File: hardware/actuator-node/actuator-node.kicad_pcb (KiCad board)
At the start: 2 copper layers, 70 x 60 mm, 60 parts, among them J1 PHASES, J2 CAN IN, J3 CAN EXT, J4 19V IN, J5 SWD, J6 ENCODER, J7 NTC, J8 SPI, U1 STM32G431CBT6, U2 SN65HVD230, U4 INA240A1D, U5 INA240A1D, U6 AMS1117-3.3, Y1 8 MHz

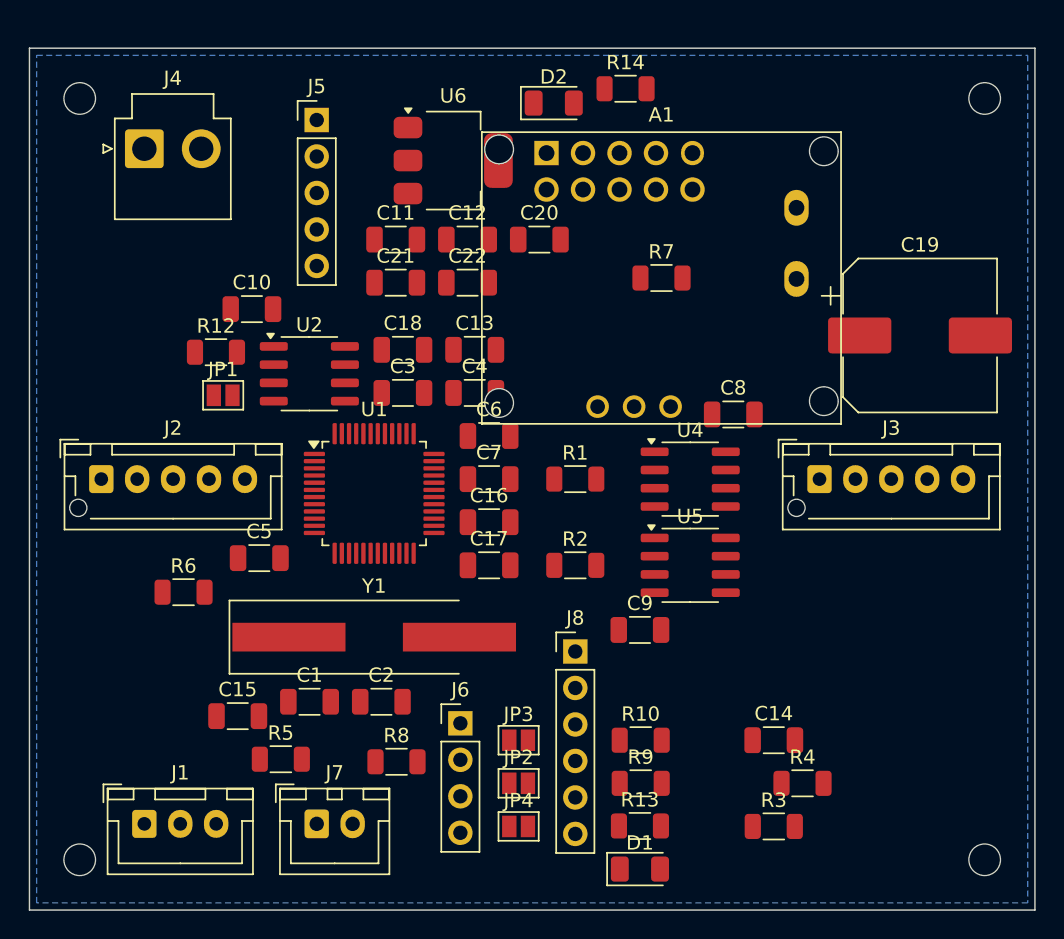
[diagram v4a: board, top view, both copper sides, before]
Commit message: Lay the node out around right-angle connectors, and spec what it can do
The connector order is all right-angle JST: 3-pin XH, 5-pin XH and 2-pin VH,
with no 2-pin XH at all. A right-angle body opens toward +Y at 0 degrees, so
the rotation is what points a cable off the board, and the placer had no
concept of rotation - it put J2 through the crystal and pushed J1 and J7 past
the outline.

kigen.rotate_boxes turns a footprint's courtyard with it; pinned entries now
take an optional third element; check.py rotates the library courtyard before
testing overlap and outline, and verifies the angle as well as the position.

Floorplan, following the three placement rules:
  - CAN on opposite edges, J2 left and J3 right
  - the whole motor loom on the bottom edge: phases, NTC, encoder, SPI
  - power and SWD on the top
All eight ports are on the perimeter, none closer than 1.1 mm to an edge.

Four things the auto-placer got wrong and are now pinned:
  - U6 sat under the driver module, stacking the LDO's heat under the bridge's
  - R7 sat on A1's exact origin; it belongs under the module, but deliberately
    placed clear of every pad rather than by accident
  - both crystal load caps sat at one end of a 20 mm hand-solder footprint,
    leaving one of them 22 mm from its terminal
  - the node-ID pull-ups were stranded 13 mm from their jumpers

Vbus divider R4 4k7 -> 10k. 100 k / 4k7 read 19 V as 0.85 V, a quarter of the
ADC span. 100 k / 10 k reads 1.73 V and clips at 36 V.

Two renderer bugs, both only visible once something was rotated or mirrored:
  - pad angles were being summed with the footprint angle, but KiCad stores a
    pad's angle absolutely
  - the mirror reflected about the origin rather than the view box, and the
    substrate rect took its min in board space instead of screen space, so the
    bottom view sat 13 mm left and grew a slab off the far edge

New docs:
  - docs/capabilities.md - bus range, torque and current resolution, loop
    rates, CAN bandwidth a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
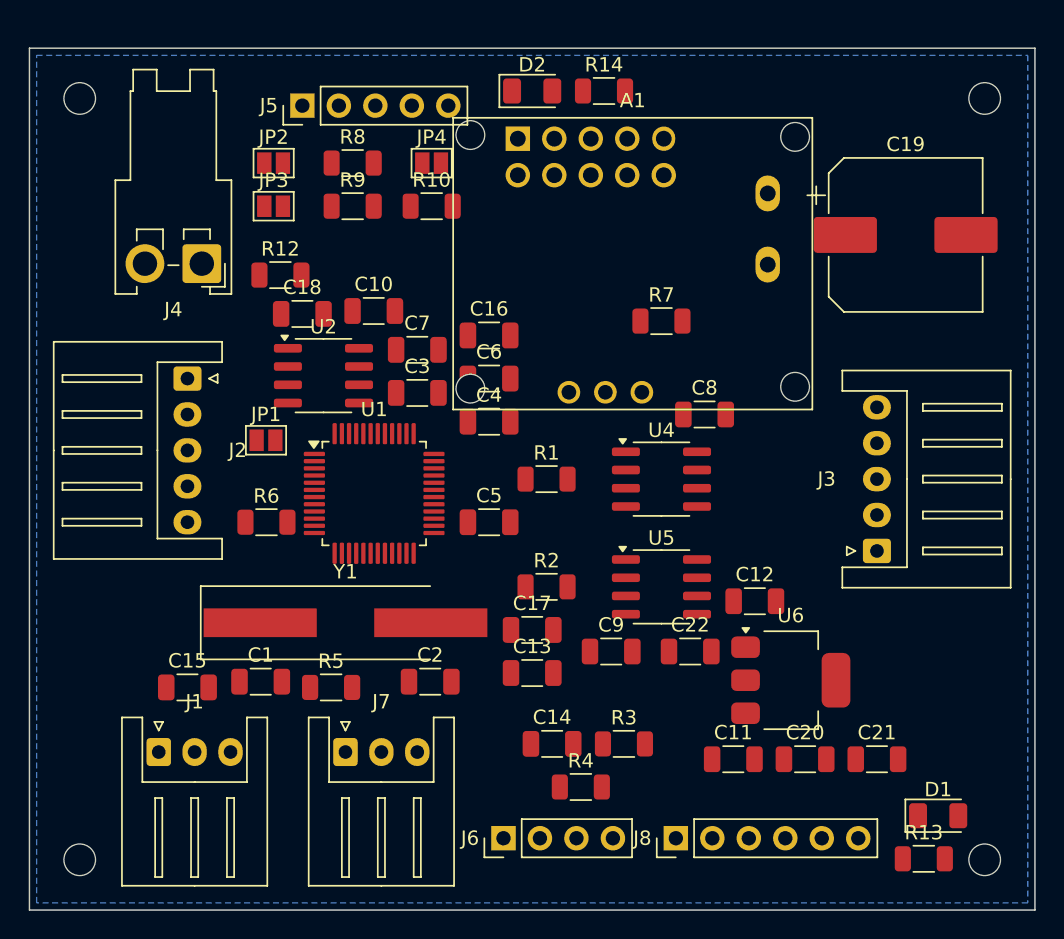
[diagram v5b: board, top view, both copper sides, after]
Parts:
- J1: footprint Connector_JST:JST_XH_B3B-XH-A_1x03_P2.50mm_Vertical -> Connector_JST:JST_XH_S3B-XH-A_1x03_P2.50mm_Horizontal
- J2, J3: footprint Connector_JST:JST_XH_B5B-XH-AM_1x05_P2.50mm_Vertical -> Connector_JST:JST_XH_S5B-XH-A_1x05_P2.50mm_Horizontal
- J4: footprint Connector_JST:JST_VH_B2P-VH_1x02_P3.96mm_Vertical -> Connector_JST:JST_VH_S2P-VH_1x02_P3.96mm_Horizontal
- J7: footprint Connector_JST:JST_XH_B2B-XH-A_1x02_P2.50mm_Vertical -> Connector_JST:JST_XH_S3B-XH-A_1x03_P2.50mm_Horizontal
- R4: value 4k7 -> 10k
- moved C21 47.1 mm to (59.0, 49.5)
- moved JP4 46.6 mm to (28.0, 8.00)
- moved JP2 46.4 mm to (17.0, 8.00)
- moved R9 44.9 mm to (22.5, 11.0)
- moved C11 43.1 mm to (49.0, 49.5)
- moved U6 43.1 mm to (53.0, 44.0)
- moved R8 41.8 mm to (22.5, 8.00)
- moved JP3 40.9 mm to (17.0, 11.0)
- moved C20 40.6 mm to (54.0, 49.5)
- moved R10 39.9 mm to (28.0, 11.0)
- moved C12 32.2 mm to (50.5, 38.5)
- moved C22 30.0 mm to (46.0, 42.0)
- moved C13 22.9 mm to (35.0, 43.5)
- moved D1 21.1 mm to (63.3, 53.4)
- moved R13 19.9 mm to (62.3, 56.4)
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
